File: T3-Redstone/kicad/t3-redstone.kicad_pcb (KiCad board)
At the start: 4 copper layers, 85 x 56 mm, 87 parts, among them J1 Gemstone 40P disi, J10 QWIIC, J11 USB-C, J12 ACIL STOP (NC), J13 BUMPER, J14 GPIO, J2 XT60 2S LiPo, J3 GEMSTONE GUC, J4 MOTOR A, J5 MOTOR B, J6 ENKODER A, J7 ENKODER B, J8A SERVO 1-8, J8B SERVO 9-16, Q1 AO4407A, Q2 AO4407A, Q3 AO3400A, Q4 AO3400A, SW1 BOOT, SW2 RESET, U1 ESP32-S3-WROOM-1U-N8R2, U10 USBLC6-2SC6, U2 DRV8874, U3 DRV8874, U4 PCA9685PW, U5 INA226, U6 AP2112K-3.3, U7 TPS563201, U8 74LVC245, U9 74AHCT1G125

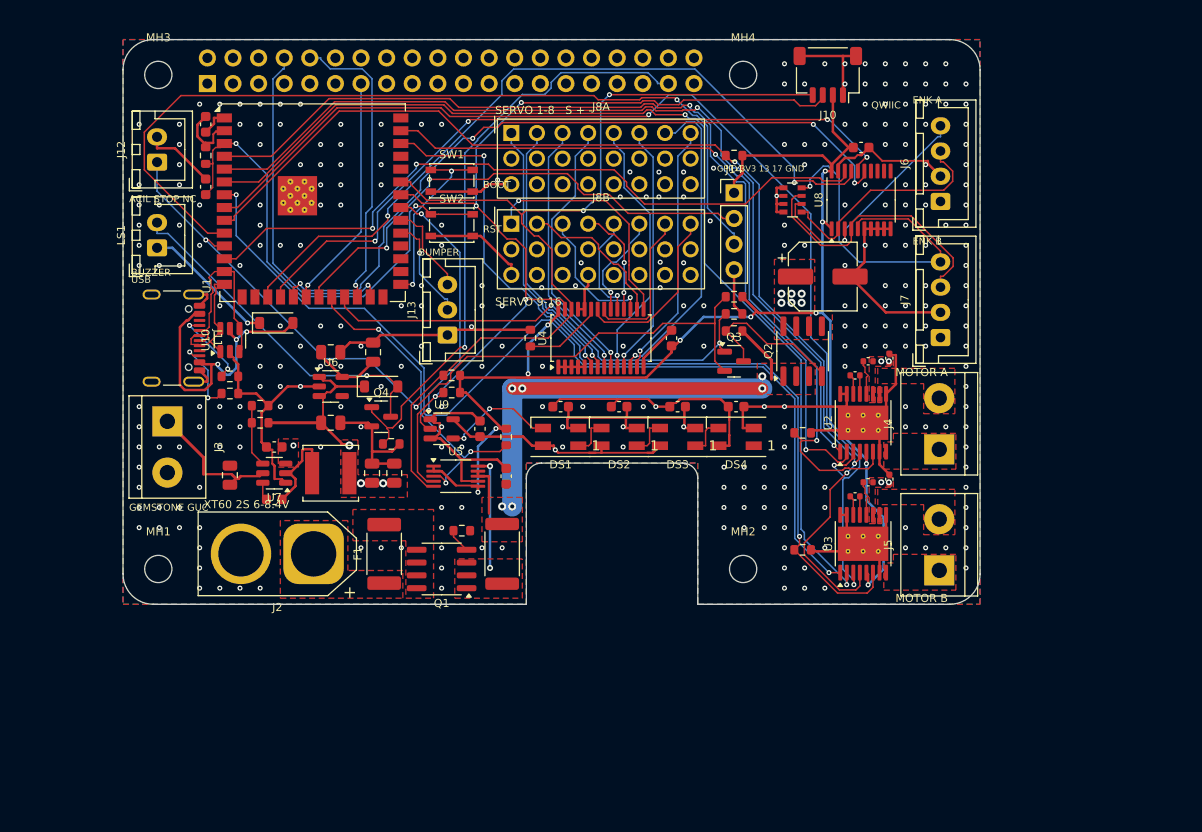
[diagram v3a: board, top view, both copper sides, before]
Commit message: T3-Redstone: guc dagitimi ve yonlendirme duzeltmeleri (ara kayit)
- +3V3 omurgasi B.Cu'ya tasindi; LDO cikisi, I2C pull-up, PCA9685, INA226 adres
  pinleri ve sag bolge icin kilitli baglantilar
- C2 / C4 ters yonluydu (3V3 pini GND tarafinda), C12 cipten 11 mm uzaktaydi
- LED +5V pinleri kesitin ustundeki F.Cu raydan birlesiyor
- USB D+/D- icin ayri net sinifi (0.1 mm aralik)
- rs_route: fanout pedin kendisini engel sayiyordu (SWIG 'is' karsilastirmasi);
  pasiflerin guc pinleri yonlendirmeden once fanout'lanir; ayni netin kopuk
  parcalarini birlestiren onarim adimi

Co-Authored-By: Claude Opus 5.5 <noreply@anthropic.com>
Claude-Session: https://claude.ai/code/session_01YQNy21SHVjiYix4RbadZre
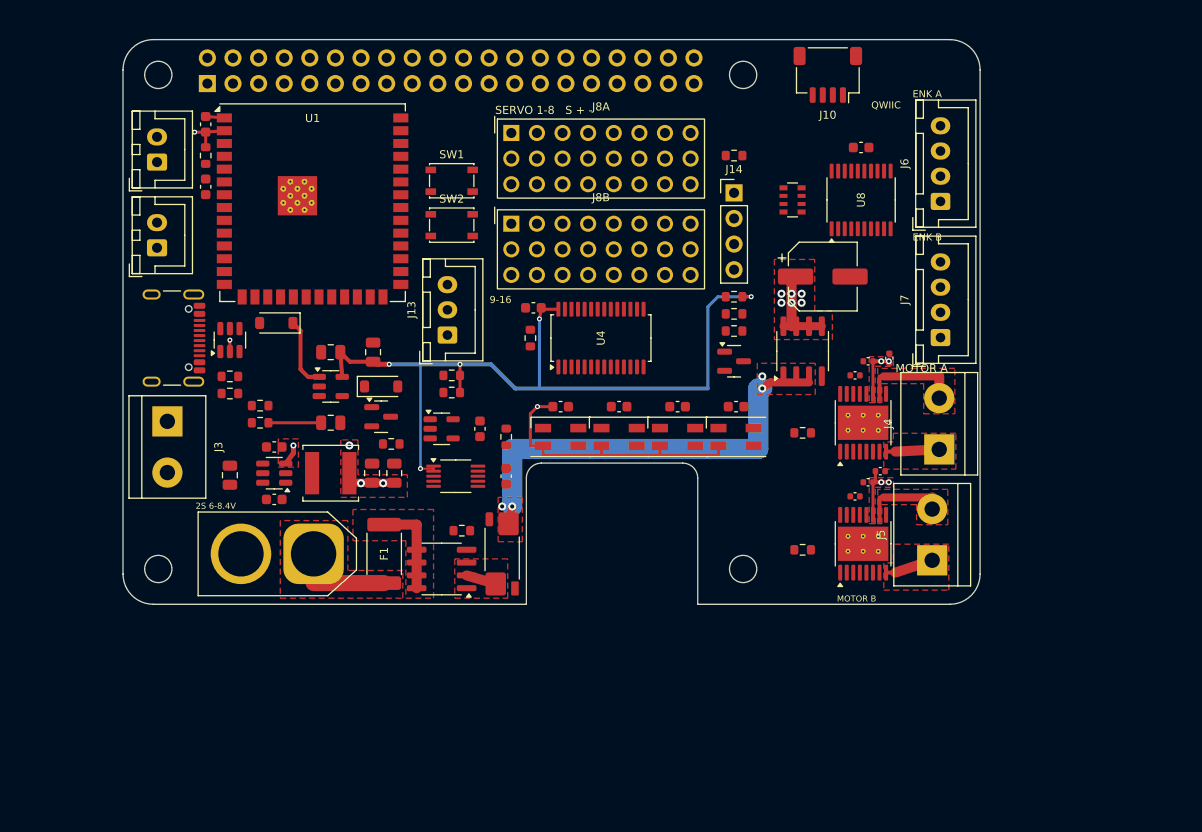
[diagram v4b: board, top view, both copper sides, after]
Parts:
- RS1: value 2m 2W -> 2m 3W; footprint Resistor_SMD:R_2512_6332Metric -> Resistor_SMD:R_Shunt_Vishay_WSK2512_6332Metric_T1.19mm
- moved C12 14.0 mm to (70.7, 56.6), turned to 180 degrees
- moved J5 1.22 mm to (110.2, 81.6)
- moved C10 1.20 mm to (105.1, 72.8), turned to 0 degrees
- turned C2 to 180 degrees
- turned C4 to 90 degrees
- turned D1 to 180 degrees
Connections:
- J14 pad 2: GPIO13 -> GPIO16
- RS1 pad 2: VSYS -> SNS_P
- U1 pad 11: ESTOP_LOOP -> (no net)
- U1 pad 12: ENC_A1 -> (no net)
- U1 pad 17: ENC_B1 -> MA_PH
- U1 pad 18: ENC_A2 -> MA_EN
- U1 pad 19: ENC_B2 -> MB_PH
- U1 pad 20: ESTOP_STAT -> MB_EN
- U1 pad 21: GPIO13 -> DRV_nSLEEP
- U1 pad 22: PWR_ALERT -> DRV_nFAULT
- U1 pad 24: HOST_RX -> LED_DATA
- U1 pad 25: HOST_TX -> PWR_ALERT
- U1 pad 31: BUMP1 -> ENC_A1
- U1 pad 32: BUMP2 -> ENC_B1
- U1 pad 33: LED_DATA -> ENC_A2
- U1 pad 34: I2C_SDA -> ENC_B2
- U1 pad 35: I2C_SCL -> I2C_SDA
- U1 pad 36: (no net) -> I2C_SCL
- U1 pad 37: (no net) -> ESTOP_STAT
- U1 pad 4: MA_PH -> HOST_RX
- U1 pad 5: MA_EN -> HOST_TX
- U1 pad 6: MB_PH -> ESTOP_LOOP
- U1 pad 7: MB_EN -> BUMP1
- U1 pad 8: DRV_nSLEEP -> BUMP2
- U1 pad 9: DRV_nFAULT -> GPIO16
- U5 pad 10: VBAT -> SNS_P
- U5 pad 8: VSYS -> SNS_N
- U5 pad 9: VSYS -> SNS_N
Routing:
- net GND: track 236.0 -> 3.00 mm, vias 287 -> 1
- net DRV_nSLEEP: track 114.2 -> 0.00 mm, vias 3 -> 0
- net DRV_nFAULT: track 113.3 -> 0.00 mm, vias 3 -> 0
- net MB_PH: track 104.4 -> 0.00 mm, vias 2 -> 0
- net MB_EN: track 98.2 -> 0.00 mm, vias 2 -> 0
- net MA_PH: track 94.2 -> 0.00 mm, vias 2 -> 0
- net I2C_SCL: track 93.7 -> 0.00 mm, vias 2 -> 0
- net I2C_SDA: track 92.2 -> 0.00 mm, vias 4 -> 0
- net MA_EN: track 90.8 -> 0.00 mm, vias 2 -> 0
- net GPIO17: track 85.9 -> 0.00 mm, vias 1 -> 0
- net IPROPI_B: track 83.5 -> 0.00 mm, vias 2 -> 0
- net ESTOP_LOOP: track 81.2 -> 0.00 mm, vias 2 -> 0
- net IPROPI_A: track 78.2 -> 0.00 mm, vias 2 -> 0
- net ENC_B1: track 75.9 -> 0.00 mm, vias 2 -> 0
- net +3V3: track 156.0 -> 83.0 mm, vias 11 -> 6
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- removed copper zone on B.Cu, net GND
- removed copper zone on F.Cu, net GND
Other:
- board text added: "2S 6-8.4V"
- board text added: "40P soket >=16mm, bu yuze parca konmaz"
- board text added: "9-16"
- board text added: "J12 ACIL STOP (NC) - kopru yoksa motor yok"
- board text added: "J14: 3V3 IO16 IO17 GND"
- board text added: "LS1 BUZZER 5V J13 BUMPER"
- board text added: "ROS 2 kontrol karti"
- board text added: "SW1 BOOT SW2 RESET J10 QWIIC"
- board text added: "T3 Gemstone O1 / 2S LiPo 6-8.4V"
- board text removed: "+"
- board text removed: "2S LiPo 6.0-8.4V - ters baglama korumali"
- board text removed: "40-pin disi soket >= 16 mm (USB-A/RJ45 uzerinden gecer)"
- board text removed: "ACIL STOP NC"
- board text removed: "Acil stop NC: J12'ye buton ya da kopru takilmazsa motorlar calismaz"
- board text removed: "BOOT"
- board text removed: "BUMPER"
- board text removed: "BUZZER"
- board text removed: "Bu yuze komponent KONMAZ (soket haric)"
- board text removed: "GEMSTONE GUC"
- board text removed: "GPIO 3V3 13 17 GND"
- board text removed: "ROS 2 robot kontrol karti / T3 Gemstone O1"
- board text removed: "RST"
- board text removed: "SERVO 9-16"
- board text removed: "USB"
- board text removed: "XT60 2S 6-8.4V"

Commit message: T3-Redstone: kart tamamen yonlendirildi, KiCad DRC temiz
- rs_route: Freerouting'in biraktigi kopuk parcalar icin 0.1 mm izgarali labirent
  yonlendirici (F.Cu / B.Cu + via, ip cekme sadelestirmesi); tek katmanli bos
  via'lar ve ucu bos yollar temizlenir
- +3V3: LDO cikisi (U6.5 -> C2 -> C3), R17 uzerinden sag bolge, C2 180 derece
- KiCad DRC: 0 ihlal, 0 baglantisiz ped, 0 footprint hatasi
- rs_render: --png bayragi cikis adi sanilmiyor; PNG onizleme eklendi
- J8A referansi Fab katmanina (SERVO yazisiyla cakisiyordu)
- README: durum ve yeniden uretme notlari

Co-Authored-By: Claude Opus 5.5 <noreply@anthropic.com>
Claude-Session: https://claude.ai/code/session_01YQNy21SHVjiYix4RbadZre
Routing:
- net GND: track 3.00 -> 122.2 mm, vias 1 -> 302
- net DRV_nSLEEP: track 0.00 -> 105.4 mm, vias 0 -> 3
- net DRV_nFAULT: track 0.00 -> 101.8 mm, vias 0 -> 5
- net I2C_SCL: track 0.00 -> 97.3 mm, vias 0 -> 2
- net I2C_SDA: track 0.00 -> 93.0 mm, vias 0 -> 5
- net IPROPI_B: track 0.00 -> 89.1 mm, vias 0 -> 2
- net +3V3: track 83.0 -> 171.6 mm, vias 6 -> 12
- net ESTOP_LOOP: track 0.00 -> 82.7 mm, vias 0 -> 1
- net MA_EN: track 0.00 -> 81.8 mm, vias 0 -> 2
- net BUZZER: track 0.00 -> 74.9 mm, vias 0 -> 2
- net MB_PH: track 0.00 -> 74.8 mm, vias 0 -> 2
- net IPROPI_A: track 0.00 -> 74.3 mm, vias 0 -> 2
- net MB_EN: track 0.00 -> 72.4 mm
- net GPIO17: track 0.00 -> 67.4 mm, vias 0 -> 1
- net MA_PH: track 0.00 -> 66.0 mm, vias 0 -> 2
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- added copper zone on B.Cu, net GND
- added copper zone on F.Cu, net GND
